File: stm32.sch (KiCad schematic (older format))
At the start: 32 parts

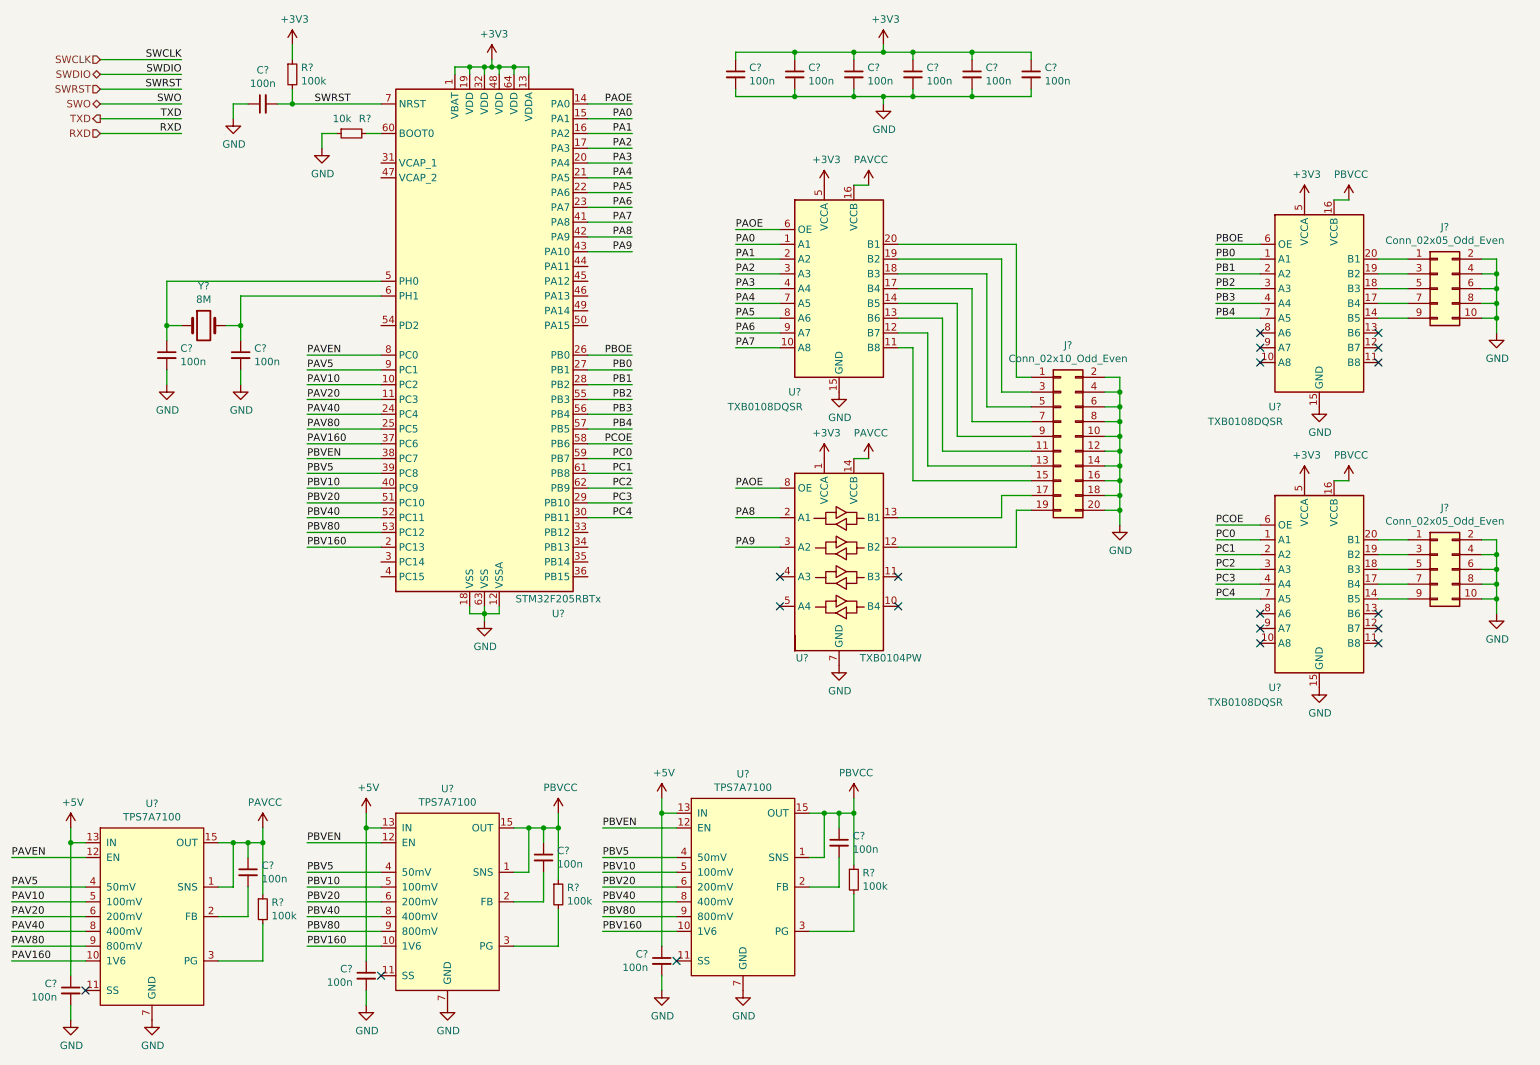
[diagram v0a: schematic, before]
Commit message: Better sch segmentation and add TCA6424A symbol
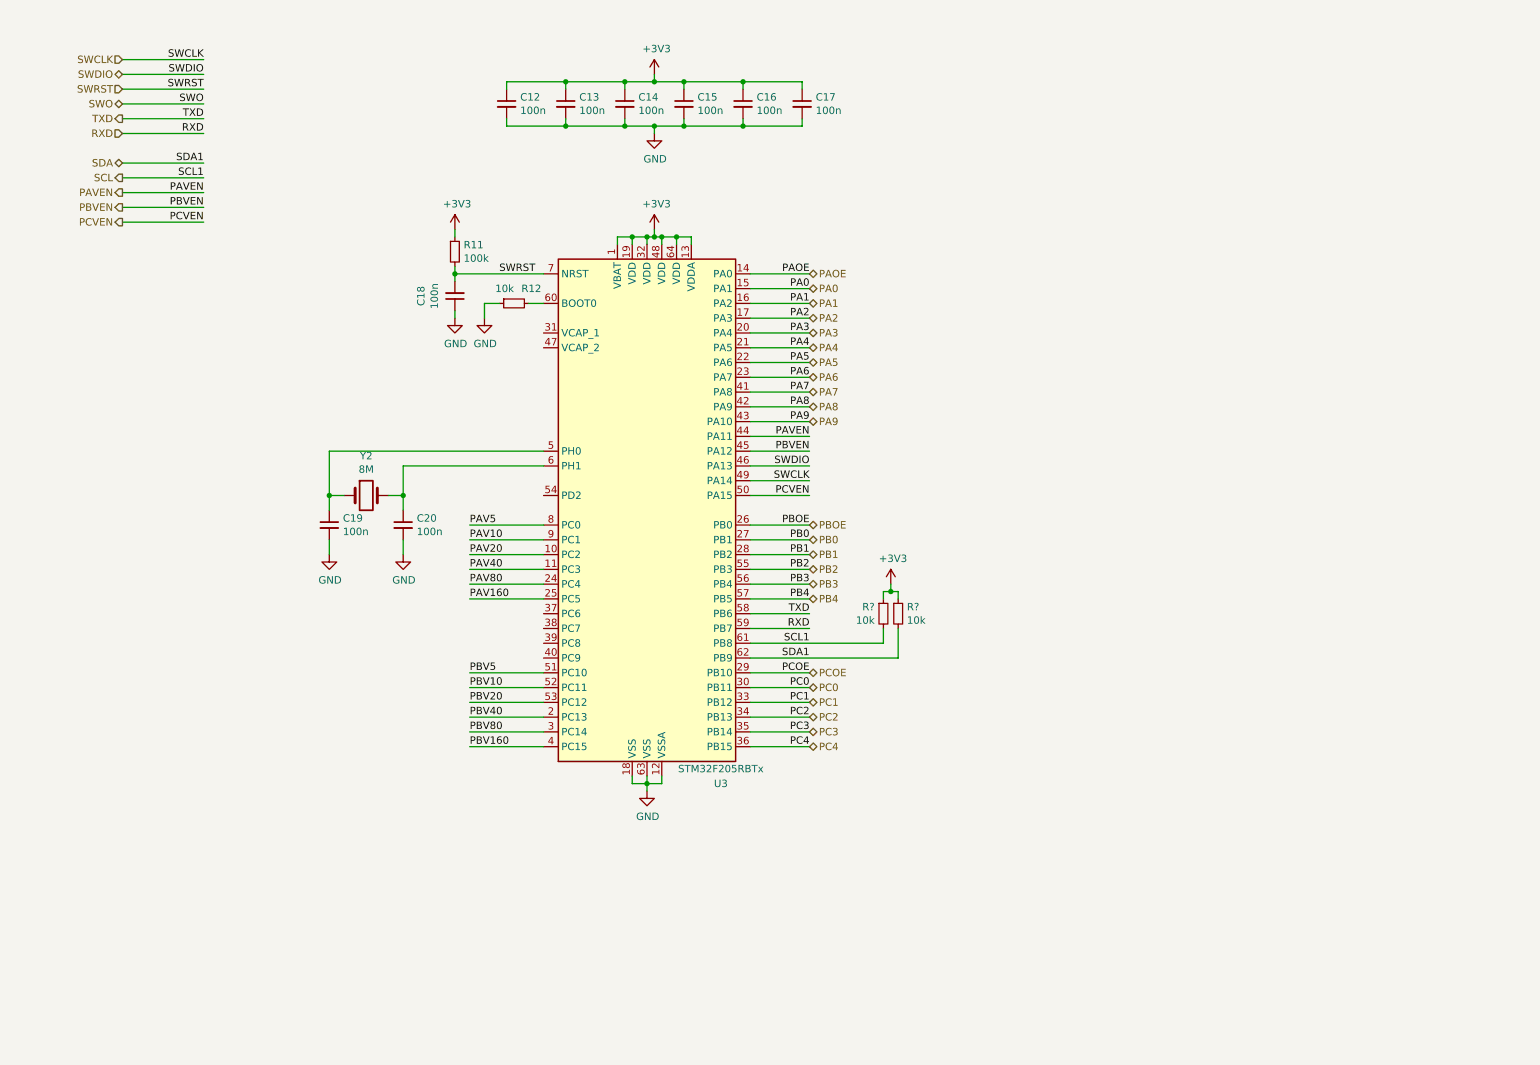
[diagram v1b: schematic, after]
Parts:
- removed C? (x6): 100n, symbol Device:C_Small
- removed J?: Conn_02x10_Odd_Even, symbol Connector_Generic:Conn_02x10_Odd_Even
- removed J? (x2): Conn_02x05_Odd_Even, symbol Connector_Generic:Conn_02x05_Odd_Even
- removed R? (x3): 100k, symbol Device:R_Small
- removed U?: TXB0104PW, Package_SO:TSSOP-14_4.4x5mm_P0.65mm, symbol Logic_LevelTranslator:TXB0104PW
- removed U? (x3): TXB0108DQSR, Package_SON:USON-20_2x4mm_P0.4mm, symbol Logic_LevelTranslator:TXB0108DQSR
- removed U? (x3): TPS7A7100, Package_DFN_QFN:VQFN-16-1EP_3x3mm_P0.5mm_EP1.6x1.6mm_ThermalVias, symbol antboard:TPS7A7100
- added R? (x2): 10k, Resistor_SMD:R_0603_1608Metric, symbol Device:R_Small
- C12, C13, C14, C15, C16, C17, C18, C19, C20: renamed from C?; footprint (none) -> Capacitor_SMD:C_0603_1608Metric
- R11, R12: renamed from R?; footprint (none) -> Resistor_SMD:R_0603_1608Metric
- Y2: renamed from Y?; footprint (none) -> Crystal:Crystal_HC52-U_Vertical
- gave numbers to parts that had none: 1
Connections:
- net +3V3: now also R?.1, R?.1
- net PAV10: now also U3.9 (PC1); no longer U3.10 (PC2)
- net PAV160: now also U3.25 (PC5); no longer U3.37 (PC6)
- net PAV20: now also U3.10 (PC2); no longer U3.11 (PC3)
- net PAV40: now also U3.11 (PC3); no longer U3.24 (PC4)
- net PAV5: now also U3.8 (PC0); no longer U3.9 (PC1)
- net PAV80: now also U3.24 (PC4); no longer U3.25 (PC5)
- net PAVEN: now also U3.44 (PA11); no longer U3.8 (PC0)
- net PBV10: now also U3.52 (PC11); no longer U3.40 (PC9)
- net PBV160: now also U3.4 (PC15); no longer U3.2 (PC13)
- net PBV20: now also U3.53 (PC12); no longer U3.51 (PC10)
- net PBV40: now also U3.2 (PC13); no longer U3.52 (PC11)
- net PBV5: now also U3.51 (PC10); no longer U3.39 (PC8)
- net PBV80: now also U3.3 (PC14); no longer U3.53 (PC12)
- net PBVEN: now also U3.45 (PA12); no longer U3.38 (PC7)
- net PC0: now also U3.30 (PB11); no longer U3.59 (PB7)
- net PC1: now also U3.33 (PB12); no longer U3.61 (PB8)
- net PC2: now also U3.34 (PB13); no longer U3.62 (PB9)
- net PC3: now also U3.35 (PB14); no longer U3.29 (PB10)
- net PC4: now also U3.36 (PB15); no longer U3.30 (PB11)
- net PCOE: now also U3.29 (PB10); no longer U3.58 (PB6)
- net RXD: now also U3.59 (PB7)
- net SWCLK: now also U3.49 (PA14)
- net SWDIO: now also U3.46 (PA13)
- net TXD: now also U3.58 (PB6)
- net PCVEN: now reaches U3.50 (PA15)
- new net SCL: R?.2, U3.61 (PB8)
- new net SDA: R?.2, U3.62 (PB9)
- no-connect marks 19 -> 0
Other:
- moved on the sheet: C12, C13, C14, C15, C16, C17, C18, C19, C20, R11, R12, U3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

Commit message: Done adding the kitchen sink
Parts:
- added C?: 100n, Capacitor_SMD:C_0603_1608Metric, symbol Device:C_Small
- added D? (x4): 19-237/R6GHBHC-A01/2T, symbol Device:LED_RGBA
- added J?: USB_C_Receptacle_USB2.0, symbol Connector:USB_C_Receptacle_USB2.0
- added R? (x2): 5k1, Resistor_SMD:R_0603_1608Metric, symbol Device:R_Small
- added R? (x3): 1k, Resistor_SMD:R_0603_1608Metric, symbol Device:R_Small
- added R?: 100k, Resistor_SMD:R_0603_1608Metric, symbol Device:R_Small
- added S?: K1-5202UA-03, antboard:K1-5202UA-03, symbol antboard:K1-5202UA-03
- added U?: OLED_0.96\"_SSD1306, antboard:OLED_0.96_SSD1306, symbol antboard:OLED_0.96"_SSD1306
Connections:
- net +3V3: now also R?.1, U?.2 (VCC)
- net GND: now also C?.1, J?.A1 (GND), J?.A12 (GND), J?.B1 (GND), J?.B12 (GND), J?.S1 (SHIELD), R?.1, R?.1, S?.5 (COM), U?.1 (GND)
- net LED_R: now reaches U3.37 (PC6)
- net LED_R: now also R?.2
- net LED_G: now reaches U3.38 (PC7)
- net LED_G: now also R?.2
- net LED_B: now reaches U3.39 (PC8)
- net LED_B: now also R?.2
- net SW0: now reaches U3.40 (PC9)
- net SW0: now also S?.1 (UP)
- net PAV10 renamed LED_A1
- net LED_A1: now also D?.4 (A)
- net PAV160 renamed SCK_~CS
- net SCK_~CS: now also U?.7 (~CS)
- net PAV20 renamed LED_A2
- net LED_A2: now also D?.4 (A)
- net PAV40 renamed LED_A3
- net LED_A3: now also D?.4 (A)
- net PAV5 renamed LED_A0
- net LED_A0: now also D?.4 (A)
- net PAV80 renamed SCR_D~C
- net SCR_D~C: now also U?.6 (D~C)
- net PAVEN renamed USB_DN
- net USB_DN: now also J?.A7 (D-), J?.B7 (D-)
- net PBV10 renamed SW1
- net SW1: now also S?.3 (LEFT)
- net PBV160 renamed SW4
- net SW4: now also S?.2 (PUSH)
- net PBV20 renamed SCR_MOSI
- net SCR_MOSI: now also U?.4 (D1)
- net PBV40 renamed SW2
- net SW2: now also S?.6 (DOWN)
- net PBV5 renamed SCR_SCK
- net SCR_SCK: now also U?.3 (D0)
- net PBV80 renamed SW3
- net SW3: now also S?.4 (RIGHT)
- net PBVEN renamed USB_DP
- net USB_DP: now also J?.A6 (D+), J?.B6 (D+)
- net PCVEN: no longer names the net of U3.50 (PA15)
- new net: J?.A5 (CC1), R?.2
- new net: J?.B5 (CC2), R?.2
- new net: D?.1 (RK), D?.1 (RK), D?.1 (RK), D?.1 (RK), R?.1
- new net: D?.2 (GK), D?.2 (GK), D?.2 (GK), D?.2 (GK), R?.1
- new net: D?.3 (BK), D?.3 (BK), D?.3 (BK), D?.3 (BK), R?.1
- new net: C?.2, R?.2, U?.5 (~RES)
- new net +5V: J?.A4 (VBUS), J?.A9 (VBUS), J?.B4 (VBUS), J?.B9 (VBUS)
- no-connect marks 0 -> 6
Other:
- moved on the sheet: C12, C13, C14, C15, C16, C17, C18, C19, C20, R11, R12, R?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

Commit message: Annotate schematic
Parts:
- D3, D4, D5, D6: renamed from D?; footprint (none) -> antboard:19-237_R6GHBHC-A01_2T
- J6: renamed from J?; footprint (none) -> Connector_USB:USB_C_Receptacle_Palconn_UTC16-G
- gave numbers to parts that had none: 11
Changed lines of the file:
@@
 P 7300 4750
 AR Path="/5DF7E971/5EA50E03" Ref="R?"  Part="1"
-AR Path="/5DFC2583/5EA50E03" Ref="R?"  Part="1"
-F 0 "R?" H 7241 4796 50  0000 R CNN
+AR Path="/5DFC2583/5EA50E03" Ref="R17"  Part="1"
+F 0 "R17" H 7241 4796 50  0000 R CNN
 F 1 "10k" H 7241 4705 50  0000 R CNN
 F 2 "Resistor_SMD:R_0603_1608Metric" H 7300 4750 50  0001 C CNN
@@
 P 7400 4750
 AR Path="/5DF7E971/5EA52602" Ref="R?"  Part="1"
-AR Path="/5DFC2583/5EA52602" Ref="R?"  Part="1"
-F 0 "R?" H 7459 4796 50  0000 L CNN
+AR Path="/5DFC2583/5EA52602" Ref="R18"  Part="1"
+F 0 "R18" H 7459 4796 50  0000 L CNN
 F 1 "10k" H 7459 4705 50  0000 L CNN
 F 2 "Resistor_SMD:R_0603_1608Metric" H 7400 4750 50  0001 C CNN
@@
 AR Path="/5EA709E1" Ref="#PWR?"  Part="1"
 AR Path="/5DF7E971/5EA709E1" Ref="#PWR?"  Part="1"
-AR Path="/5DFC2583/5EA709E1" Ref="#PWR?"  Part="1"
-F 0 "#PWR?" H 7350 4400 50  0001 C CNN
+AR Path="/5DFC2583/5EA709E1" Ref="#PWR05"  Part="1"
+F 0 "#PWR05" H 7350 4400 50  0001 C CNN
 F 1 "+3V3" H 7365 4723 50  0000 C CNN
 F 2 "" H 7350 4550 50  0001 C CNN
@@
 NoConn ~ 6400 3950
 $Comp
-L Connector:USB_C_Receptacle_USB2.0 J?
+L Connector:USB_C_Receptacle_USB2.0 J6
 U 1 1 5DECBA68
 P 9300 3550
-F 0 "J?" H 8870 3489 50  0000 R CNN
+F 0 "J6" H 8870 3489 50  0000 R CNN
 F 1 "USB_C_Receptacle_USB2.0" H 8870 3398 50  0000 R CNN
-F 2 "" H 9450 3550 50  0001 C CNN
+F 2 "Connector_USB:USB_C_Receptacle_Palconn_UTC16-G" H 9450 3550 50  0001 C CNN
 F 3 "https://www.usb.org/sites/default/files/documents/usb_type-c.zip" H 9450 3550 50  0001 C CNN
 	1    9300 3550
@@
 P 8500 3150
 AR Path="/5DF7E971/5DEF366C" Ref="R?"  Part="1"
-AR Path="/5DFC2583/5DEF366C" Ref="R?"  Part="1"
-F 0 "R?" V 8400 3100 50  0000 R CNN
+AR Path="/5DFC2583/5DEF366C" Ref="R19"  Part="1"
+F 0 "R19" V 8400 3100 50  0000 R CNN
 F 1 "5k1" V 8400 3150 50  0000 L CNN
 F 2 "Resistor_SMD:R_0603_1608Metric" H 8500 3150 50  0001 C CNN
@@
 P 8500 3250
 AR Path="/5DF7E971/5DEF4157" Ref="R?"  Part="1"
-AR Path="/5DFC2583/5DEF4157" Ref="R?"  Part="1"
-F 0 "R?" V 8400 3200 50  0000 R CNN
+AR Path="/5DFC2583/5DEF4157" Ref="R20"  Part="1"
+F 0 "R20" V 8400 3200 50  0000 R CNN
 F 1 "5k1" V 8400 3250 50  0000 L CNN
 F 2 "Resistor_SMD:R_0603_1608Metric" H 8500 3250 50  0001 C CNN
@@
 	8300 3250 8400 3250
 $Comp
-L power:GND #PWR?
+L power:GND #PWR06
 U 1 1 5DF03FFD
 P 8300 3300
-F 0 "#PWR?" H 8300 3050 50  0001 C CNN
+F 0 "#PWR06" H 8300 3050 50  0001 C CNN
 F 1 "GND" H 8305 3127 50  0000 C CNN
 F 2 "" H 8300 3300 50  0001 C CNN
@@
 Connection ~ 8300 3250
 $Comp
-L power:GND #PWR?
+L power:GND #PWR08
 U 1 1 5DF08A10
 P 9450 4550
-F 0 "#PWR?" H 9450 4300 50  0001 C CNN
+F 0 "#PWR08" H 9450 4300 50  0001 C CNN
 F 1 "GND" H 9455 4377 50  0000 C CNN
 F 2 "" H 9450 4550 50  0001 C CNN
@@
 	9450 4500 9600 4500
 $Comp
-L power:+5V #PWR?
+L power:+5V #PWR07
 U 1 1 5DF12003
 P 8600 2850
-F 0 "#PWR?" H 8600 2700 50  0001 C CNN
+F 0 "#PWR07" H 8600 2700 50  0001 C CNN
 F 1 "+5V" H 8615 3023 50  0000 C CNN
 F 2 "" H 8600 2850 50  0001 C CNN
@@
 LED_A3
 $Comp
-L Device:LED_RGBA D?
+L Device:LED_RGBA D6
 U 1 1 5E06E532
 P 3250 7050
-F 0 "D?" V 3450 7350 50  0000 R CNN
+F 0 "D6" V 3450 7350 50  0000 R CNN
 F 1 "19-237/R6GHBHC-A01/2T" V 4050 6650 50  0001 R CNN
-F 2 "" H 3250 7000 50  0001 C CNN
+F 2 "antboard:19-237_R6GHBHC-A01_2T" H 3250 7000 50  0001 C CNN
 F 3 "~" H 3250 7000 50  0001 C CNN
 	1    3250 7050
@@
 $EndComp
 $Comp
-L Device:LED_RGBA D?
+L Device:LED_RGBA D5
 U 1 1 5E06D7A2
 P 2500 7050
-F 0 "D?" V 2700 7350 50  0000 R CNN
+F 0 "D5" V 2700 7350 50  0000 R CNN
 F 1 "19-237/R6GHBHC-A01/2T" V 3300 6650 50  0001 R CNN
-F 2 "" H 2500 7000 50  0001 C CNN
+F 2 "antboard:19-237_R6GHBHC-A01_2T" H 2500 7000 50  0001 C CNN
 F 3 "~" H 2500 7000 50  0001 C CNN
 	1    2500 7050
@@
 $EndComp
 $Comp
-L Device:LED_RGBA D?
+L Device:LED_RGBA D4
 U 1 1 5E06BB7B
 P 1750 7050
-F 0 "D?" V 1950 7350 50  0000 R CNN
+F 0 "D4" V 1950 7350 50  0000 R CNN
 F 1 "19-237/R6GHBHC-A01/2T" V 2550 6650 50  0001 R CNN
-F 2 "" H 1750 7000 50  0001 C CNN
+F 2 "antboard:19-237_R6GHBHC-A01_2T" H 1750 7000 50  0001 C CNN
 F 3 "~" H 1750 7000 50  0001 C CNN
 	1    1750 7050
@@
 	1000 6850 1000 6550
 $Comp
-L Device:LED_RGBA D?
+L Device:LED_RGBA D3
 U 1 1 5DF6533B
 P 1000 7050
-F 0 "D?" V 1200 7350 50  0000 R CNN
+F 0 "D3" V 1200 7350 50  0000 R CNN
 F 1 "19-237/R6GHBHC-A01/2T" V 1800 6650 50  0000 R CNN
-F 2 "" H 1000 7000 50  0001 C CNN
+F 2 "antboard:19-237_R6GHBHC-A01_2T" H 1000 7000 50  0001 C CNN
 F 3 "~" H 1000 7000 50  0001 C CNN
 	1    1000 7050
@@
 	9900 5350 10000 5350
 $Comp
-L power:GND #PWR?
+L power:GND #PWR09
 U 1 1 5DF22FB4
 P 10000 5450
-F 0 "#PWR?" H 10000 5200 50  0001 C CNN
+F 0 "#PWR09" H 10000 5200 50  0001 C CNN
 F 1 "GND" H 10005 5277 50  0000 C CNN
 F 2 "" H 10000 5450 50  0001 C CNN
@@
 $EndComp
 $Comp
-L antboard:K1-5202UA-03 S?
+L antboard:K1-5202UA-03 S1
 U 1 1 5DF218C7
 P 8900 5050
-F 0 "S?" H 9350 5215 50  0000 C CNN
+F 0 "S1" H 9350 5215 50  0000 C CNN
 F 1 "K1-5202UA-03" H 9350 5124 50  0000 C CNN
 F 2 "antboard:K1-5202UA-03" H 8900 5050 50  0001 C CNN
@@
 P 3750 7350
 AR Path="/5DF7E971/5E2945B4" Ref="R?"  Part="1"
-AR Path="/5DFC2583/5E2945B4" Ref="R?"  Part="1"
-F 0 "R?" V 3700 7250 50  0000 R CNN
+AR Path="/5DFC2583/5E2945B4" Ref="R14"  Part="1"
+F 0 "R14" V 3700 7250 50  0000 R CNN
 F 1 "1k" V 3700 7450 50  0000 L CNN
 F 2 "Resistor_SMD:R_0603_1608Metric" H 3750 7350 50  0001 C CNN
@@
 P 3750 7450
 AR Path="/5DF7E971/5E295ACD" Ref="R?"  Part="1"
-AR Path="/5DFC2583/5E295ACD" Ref="R?"  Part="1"
-F 0 "R?" V 3700 7350 50  0000 R CNN
+AR Path="/5DFC2583/5E295ACD" Ref="R15"  Part="1"
+F 0 "R15" V 3700 7350 50  0000 R CNN
 F 1 "1k" V 3700 7550 50  0000 L CNN
 F 2 "Resistor_SMD:R_0603_1608Metric" H 3750 7450 50  0001 C CNN
@@
 P 3750 7550
 AR Path="/5DF7E971/5E295D66" Ref="R?"  Part="1"
-AR Path="/5DFC2583/5E295D66" Ref="R?"  Part="1"
-F 0 "R?" V 3700 7450 50  0000 R CNN
+AR Path="/5DFC2583/5E295D66" Ref="R16"  Part="1"
+F 0 "R16" V 3700 7450 50  0000 R CNN
 F 1 "1k" V 3700 7650 50  0000 L CNN
 F 2 "Resistor_SMD:R_0603_1608Metric" H 3750 7550 50  0001 C CNN
@@
 $EndComp
 $Comp
-L antboard:OLED_0.96"_SSD1306 U?
+L antboard:OLED_0.96"_SSD1306 U4
 U 1 1 5E2A046D
 P 2150 4700
-F 0 "U?" H 2577 4446 50  0000 L CNN
+F 0 "U4" H 2577 4446 50  0000 L CNN
 F 1 "OLED_0.96\"_SSD1306" H 2577 4355 50  0000 L CNN
 F 2 "antboard:OLED_0.96_SSD1306" H 1300 4700 50  0001 C CNN
@@
 AR Path="/5E3156D1" Ref="#PWR?"  Part="1"
 AR Path="/5DF7E971/5E3156D1" Ref="#PWR?"  Part="1"
-AR Path="/5DFC2583/5E3156D1" Ref="#PWR?"  Part="1"
-F 0 "#PWR?" H 2800 5250 50  0001 C CNN
+AR Path="/5DFC2583/5E3156D1" Ref="#PWR04"  Part="1"
+F 0 "#PWR04" H 2800 5250 50  0001 C CNN
 F 1 "GND" H 2805 5327 50  0000 C CNN
 F 2 "" H 2800 5500 50  0001 C CNN
@@
 P 2800 4500
 AR Path="/5DF7E971/5E3156C8" Ref="#PWR?"  Part="1"
-AR Path="/5DFC2583/5E3156C8" Ref="#PWR?"  Part="1"
-F 0 "#PWR?" H 2800 4350 50  0001 C CNN
+AR Path="/5DFC2583/5E3156C8" Ref="#PWR03"  Part="1"
+F 0 "#PWR03" H 2800 4350 50  0001 C CNN
 F 1 "+3V3" H 2815 4673 50  0000 C CNN
 F 2 "" H 2800 4500 50  0001 C CNN
@@
 AR Path="/5E3156C2" Ref="C?"  Part="1"
 AR Path="/5DF7E971/5E3156C2" Ref="C?"  Part="1"
-AR Path="/5DFC2583/5E3156C2" Ref="C?"  Part="1"
-F 0 "C?" V 2571 5250 50  0000 C CNN
+AR Path="/5DFC2583/5E3156C2" Ref="C21"  Part="1"
+F 0 "C21" V 2571 5250 50  0000 C CNN
 F 1 "100n" V 2662 5250 50  0000 C CNN
 F 2 "Capacitor_SMD:C_0603_1608Metric" H 2800 5250 50  0001 C CNN
@@
 P 2800 4750
 AR Path="/5DF7E971/5E3156BC" Ref="R?"  Part="1"
-AR Path="/5DFC2583/5E3156BC" Ref="R?"  Part="1"
-F 0 "R?" H 2859 4796 50  0000 L CNN
+AR Path="/5DFC2583/5E3156BC" Ref="R13"  Part="1"
+F 0 "R13" H 2859 4796 50  0000 L CNN
 F 1 "100k" H 2859 4705 50  0000 L CNN
 F 2 "Resistor_SMD:R_0603_1608Metric" H 2800 4750 50  0001 C CNN
@@
 AR Path="/5E344111" Ref="#PWR?"  Part="1"
 AR Path="/5DF7E971/5E344111" Ref="#PWR?"  Part="1"
-AR Path="/5DFC2583/5E344111" Ref="#PWR?"  Part="1"
-F 0 "#PWR?" H 1850 5250 50  0001 C CNN
+AR Path="/5DFC2583/5E344111" Ref="#PWR02"  Part="1"
+F 0 "#PWR02" H 1850 5250 50  0001 C CNN
 F 1 "GND" H 1855 5327 50  0000 C CNN
 F 2 "" H 1850 5500 50  0001 C CNN
@@
 P 1850 4500
 AR Path="/5DF7E971/5E344634" Ref="#PWR?"  Part="1"
-AR Path="/5DFC2583/5E344634" Ref="#PWR?"  Part="1"
-F 0 "#PWR?" H 1850 4350 50  0001 C CNN
+AR Path="/5DFC2583/5E344634" Ref="#PWR01"  Part="1"
+F 0 "#PWR01" H 1850 4350 50  0001 C CNN
 F 1 "+3V3" H 1865 4673 50  0000 C CNN
 F 2 "" H 1850 4500 50  0001 C CNN

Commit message: Schematic mostly done, place begun
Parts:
- Y2: footprint Crystal:Crystal_HC52-U_Vertical -> Crystal:Crystal_HC18-U_Vertical
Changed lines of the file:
@@
 F 0 "Y2" H 3800 4218 50  0000 C CNN
 F 1 "8M" H 3800 4127 50  0000 C CNN
-F 2 "Crystal:Crystal_HC52-U_Vertical" H 3800 3950 50  0001 C CNN
+F 2 "Crystal:Crystal_HC18-U_Vertical" H 3800 3950 50  0001 C CNN
 F 3 "~" H 3800 3950 50  0001 C CNN
 	1    3800 3950
